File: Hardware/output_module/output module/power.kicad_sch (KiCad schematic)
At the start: 16 parts, among them J1 euro_power_16, U2 TL074, U3 TL074

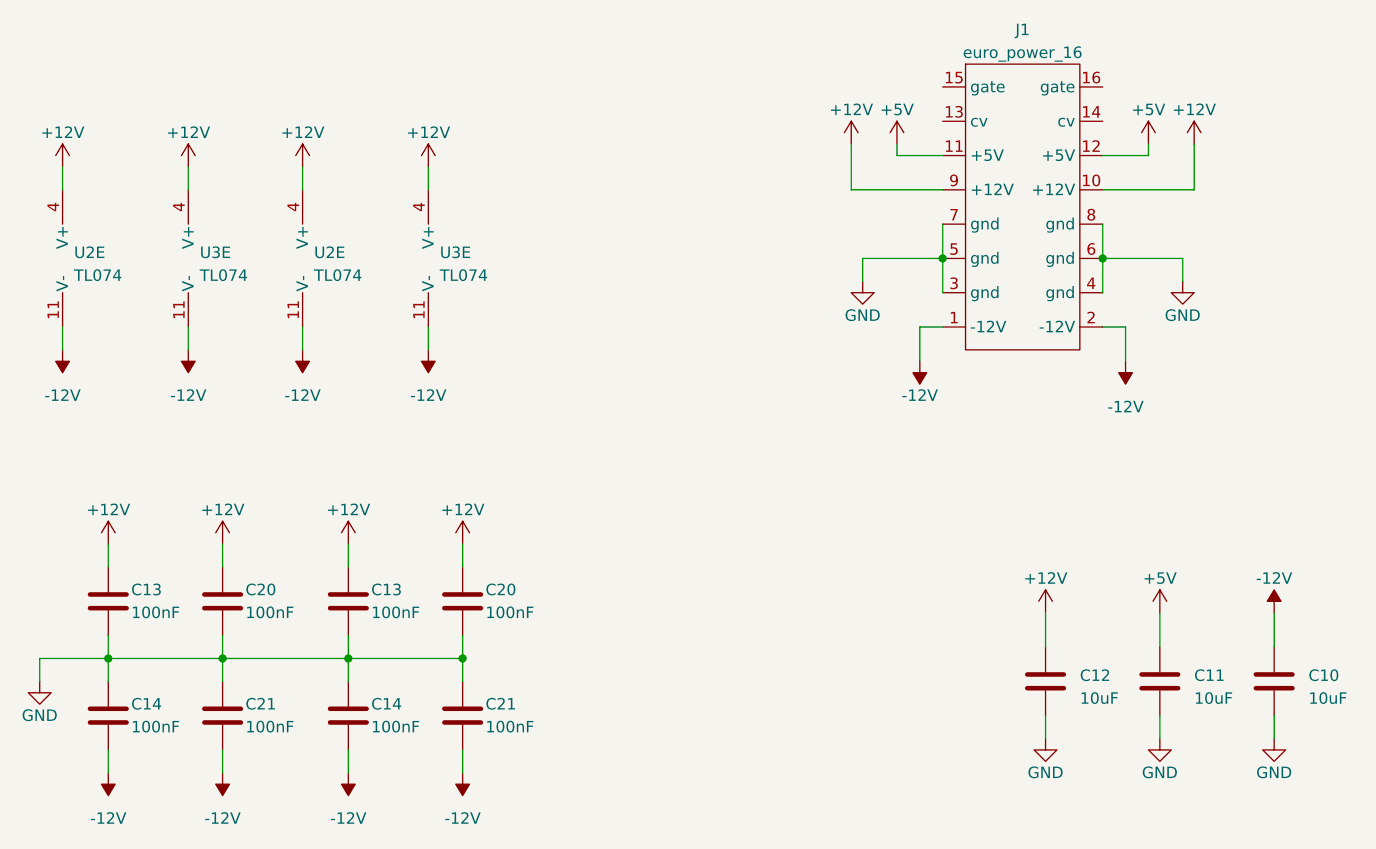
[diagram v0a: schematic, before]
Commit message: proto order
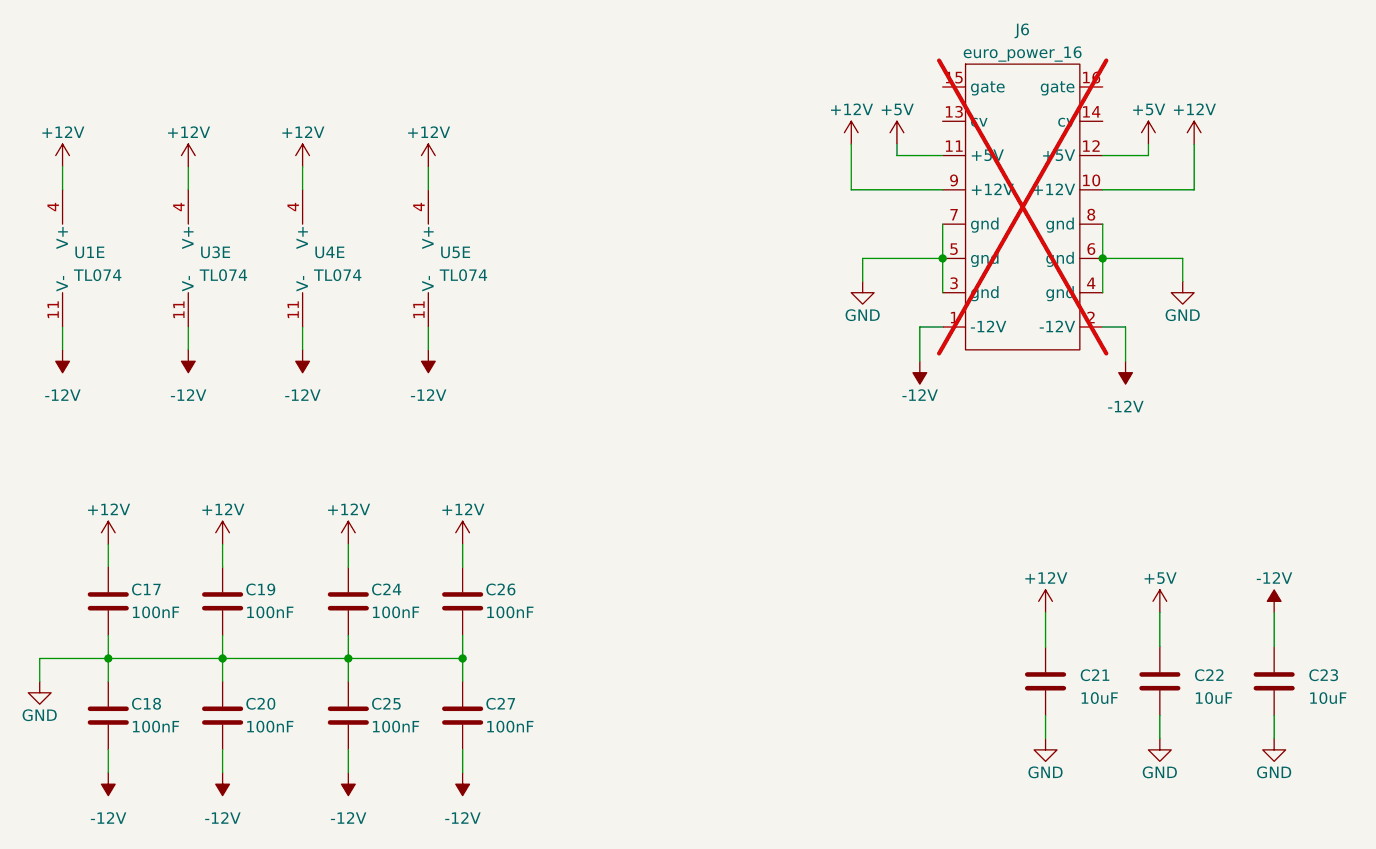
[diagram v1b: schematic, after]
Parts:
- J6: renamed from J1; now not fitted
- renumbered C13 to C17, C14 to C18, C20 to C19, C21 to C20, C12 to C21, C11 to C22, C10 to C23, C13 to C24, C14 to C25, C20 to C26, C21 to C27, U2 to U1, U2 to U4, U3 to U5

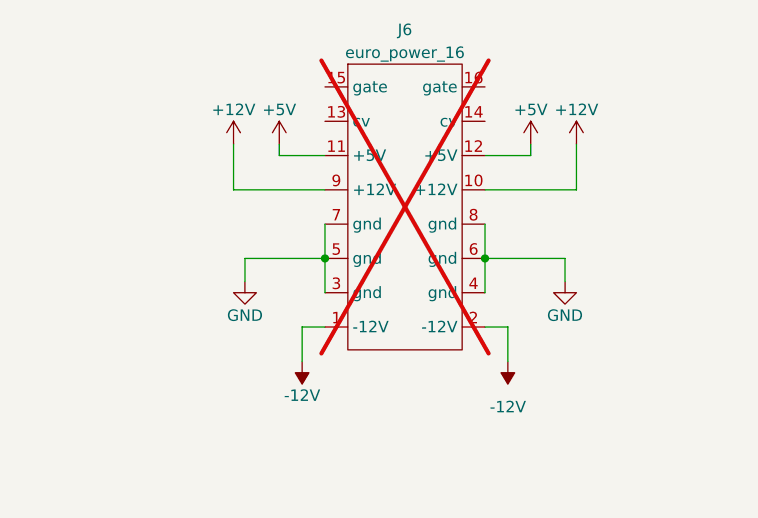
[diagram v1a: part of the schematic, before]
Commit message: update output module production mistakes
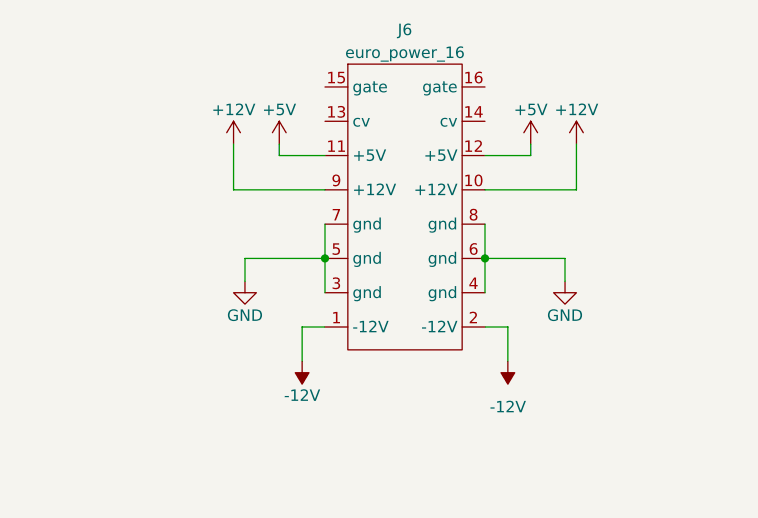
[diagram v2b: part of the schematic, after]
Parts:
- J6: now fitted
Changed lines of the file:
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@@
 		(in_bom yes)
 		(on_board yes)
-		(dnp yes)
+		(dnp no)
 		(fields_autoplaced yes)
 		(property "Reference" "J6"
